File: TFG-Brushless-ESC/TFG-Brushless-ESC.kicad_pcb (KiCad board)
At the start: 4 copper layers, 130 x 50 mm, 113 parts, among them J1 24V IN, J2 MOTOR, J5 USB C Receptacle, J6 HALL SENSORS, J7 SWD, M3 MountingHole_3.2mm_M3_Pad_Via, Q1 TK58E06N1, Q2 TK58E06N1, Q3 TK58E06N1, Q4 TK58E06N1, Q5 TK58E06N1, Q6 TK58E06N1, SW1 BOOT0, SW2 NRST, U1 LM317, U2 LM317, U3 STM32F411CEUx, U4 IR2101, U5 INA180A3, U6 IR2101, U7 INA180A3, U8 IR2101, U9 INA180A3, Y1 25MHz, Y2 32.768kHz

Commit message: temporary unifinished layout
tht components and initia layout
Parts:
- removed C41: 100n, Capacitor_SMD:C_0603_1608Metric
- removed C42: 10p, Capacitor_SMD:C_0603_1608Metric
- removed J7: SWD, Connector_PinHeader_2.54mm:PinHeader_1x04_P2.54mm_Vertical
- removed the M3 at (234.0, 138.0)
- removed the M3 at (234.0, 98.0)
- removed the M3 at (114.0, 98.0)
- removed the M3 at (114.0, 138.0)
- removed R36: 10k, Resistor_SMD:R_0603_1608Metric
- added ?: , , F.Cu at (139.3, 161.1)
- added C11: 100n, Capacitor_SMD:C_0603_1608Metric, F.Cu at (82.1, 175.2)
- added D11: SMAJ16CA-13-F, Diode_SMD:D_SMA, F.Cu at (94.1, 140.9)
- added D12: 1N4148, Diode_SMD:D_SOD-123, F.Cu at (119.1, 132.3)
- added D13: SMAJ16CA-13-F, Diode_SMD:D_SMA, F.Cu at (131.2, 140.8)
- added D5: B240A-13-F, Diode_SMD:D_SMA, F.Cu at (130.0, 149.4)
- added D8: 1N4148, Diode_SMD:D_SOD-123, F.Cu at (54.5, 132.3)
- added F1: 15 A, TFG-Brushless-ESC:Fuseholder_Automotive, F.Cu at (64.9, 153.0)
- added F2: 2A, Fuse:Fuse_1812_4532Metric, F.Cu at (124.5, 153.4)
- added J3: SWD, Connector_PinHeader_2.54mm:PinHeader_1x04_P2.54mm_Vertical, F.Cu at (98.1, 186.9)
- added J4: HALL SENSORS, Connector_JST:JST_PH_B5B-PH-SM4-TB_1x05-1MP_P2.00mm_Vertical, F.Cu at (103.1, 162.2)
- added M3: MountingHole_3.2mm_M3_Pad_Via, MountingHole:MountingHole_3.2mm_M3_Pad_Via, F.Cu at (139.3, 161.1)
- added M3: MountingHole_3.2mm_M3_Pad_Via, MountingHole:MountingHole_3.2mm_M3_Pad_Via, F.Cu at (49.3, 161.1)
- added R13: 10k, Resistor_SMD:R_0603_1608Metric, F.Cu at (100.3, 157.0)
- C13: value 100n -> 20p
- C15: value 20p -> 12p5
- C17: value 12p5 -> 2u2
- C18: value 2u2 -> 10u; footprint Capacitor_SMD:C_0603_1608Metric -> Capacitor_THT:CP_Radial_D5.0mm_P2.00mm
- C19: value 2.2u -> 2u2
- C20: value 100n -> 2.2u; footprint Capacitor_SMD:C_0603_1608Metric -> Capacitor_THT:CP_Radial_D5.0mm_P2.00mm
- C21, C38: value 47u -> 100n; footprint Capacitor_THT:CP_Radial_D5.0mm_P2.00mm -> Capacitor_SMD:C_0603_1608Metric
- C23, C36: value 100n -> 47u; footprint Capacitor_SMD:C_0603_1608Metric -> Capacitor_THT:CP_Radial_D5.0mm_P2.00mm
- C24, C32: value 10u -> 100n; footprint Capacitor_THT:CP_Radial_D5.0mm_P2.00mm -> Capacitor_SMD:C_0603_1608Metric
- C33: value 100n -> 10p
- C34: value 10p -> 2.2u; footprint Capacitor_SMD:C_0603_1608Metric -> Capacitor_THT:CP_Radial_D5.0mm_P2.00mm
- C35: value 2.2u -> 100n; footprint Capacitor_THT:CP_Radial_D5.0mm_P2.00mm -> Capacitor_SMD:C_0603_1608Metric
- C40: value 10u -> 10p; footprint Capacitor_THT:CP_Radial_D5.0mm_P2.00mm -> Capacitor_SMD:C_0603_1608Metric
- D1: value GREEN -> D5V0L2B3T; footprint LED_SMD:LED_0805_2012Metric -> Package_TO_SOT_SMD:SOT-523
- D10: value FERD30H100SB -> 1N4148; footprint Package_TO_SOT_SMD:TO-252-2 -> Diode_SMD:D_SOD-123
- D3: value 1N4148 -> GREEN; footprint Diode_SMD:D_SOD-123 -> LED_SMD:LED_0805_2012Metric
- D6, D9: value 1N4148 -> SMAJ16CA-13-F; footprint Diode_SMD:D_SOD-123 -> Diode_SMD:D_SMA
- D7: value FERD30H100SB -> DESD5V0U1BA; footprint Package_TO_SOT_SMD:TO-252-2 -> Diode_SMD:D_SOD-323_HandSoldering
- J1: value 24V IN -> MOTOR; footprint TerminalBlock_Phoenix:TerminalBlock_Phoenix_MKDS-1,5-2-5.08_1x02_P5.08mm_Horizontal -> TerminalBlock_Phoenix:TerminalBlock_Phoenix_MKDS-1,5-3-5.08_1x03_P5.08mm_Horizontal
- J2: value MOTOR -> USB C Receptacle; footprint TerminalBlock_Phoenix:TerminalBlock_Phoenix_MKDS-1,5-3-5.08_1x03_P5.08mm_Horizontal -> Connector_USB:USB_C_Receptacle_G-Switch_GT-USB-7010ASV
- J5: value USB C Receptacle -> I2C; footprint Connector_USB:USB_C_Receptacle_G-Switch_GT-USB-7010ASV -> Connector_PinHeader_2.54mm:PinHeader_1x04_P2.54mm_Horizontal
- J6: value HALL SENSORS -> 24V IN; footprint Connector_JST:JST_PH_B5B-PH-SM4-TB_1x05-1MP_P2.00mm_Vertical -> TerminalBlock_Phoenix:TerminalBlock_Phoenix_MKDS-1,5-2-5.08_1x02_P5.08mm_Horizontal
- R14, R15, R19, R25, R31: value 1k -> 10k
- R16: value 100R -> 1k; footprint Resistor_SMD:R_0805_2012Metric -> Resistor_SMD:R_0603_1608Metric
- R17, R21, R27, R33: value 10k -> 1k
- R2: value 390R 1% -> 10k
- R20, R26, R32: value 2mR -> 100R; footprint Resistor_SMD:R_2512_6332Metric -> Resistor_SMD:R_0805_2012Metric
- R22, R28: value 100R -> 2mR; footprint Resistor_SMD:R_0805_2012Metric -> Resistor_SMD:R_2512_6332Metric
- R34: value 10k -> 2mR; footprint Resistor_SMD:R_0603_1608Metric -> Resistor_SMD:R_2512_6332Metric
- R5: value 10k -> 390R 1%
- U1: value LM317 -> LM317L_SOT-89; footprint Package_TO_SOT_THT:TO-220-3_Vertical -> Package_TO_SOT_SMD:SOT-89-3
- moved J6 185.1 mm to (56.4, 161.8), turned to 0 degrees
- moved D4 170.4 mm to (49.7, 147.3), turned to 180 degrees
- moved Q1 163.6 mm to (50.4, 123.8), turned to 0 degrees
- moved C21 157.0 mm to (54.2, 135.4)
- moved C20 154.4 mm to (50.4, 136.3)
- moved C22 150.3 mm to (50.4, 130.6)
- moved R18 149.6 mm to (51.3, 126.4), turned to 180 degrees
- moved U4 145.9 mm to (58.5, 132.3), turned to 90 degrees
- moved C24 143.9 mm to (75.8, 126.3), turned to 0 degrees
- moved Q2 139.8 mm to (61.6, 123.8), turned to 0 degrees
- moved R20 135.3 mm to (60.5, 126.4), turned to 0 degrees
- moved C23 133.9 mm to (67.1, 136.1), turned to 0 degrees
- moved U5 127.6 mm to (72.1, 125.3)
- moved R21 126.9 mm to (71.6, 129.6), turned to 0 degrees
- moved C25 121.2 mm to (71.6, 127.9), turned to 180 degrees
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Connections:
- C12 pad 1: /VDDA -> GND
- C12 pad 2: GND -> /BOOT0
- C13 pad 1: GND -> /HSE_1
- C13 pad 2: /NRST -> GND
- C14 pad 1: /HSE_1 -> /HSE_2
- C15 pad 1: /HSE_2 -> /LSE_1
- C16 pad 1: /LSE_1 -> /LSE_2
- C17 pad 1: /LSE_2 -> /VCAP1
- C18 pad 1: /VCAP1 -> +24V
- C19 pad 1: +12V -> +5V
- C21 pad 1: Net-(D3-K) -> +12V
- C21 pad 2: /U -> GND
- C22 pad 1: /U -> Net-(D8-K)
- C22 pad 2: GND -> /U
- C23 pad 1: +3V3 -> /U
- C24 pad 1: +24V -> +3V3
- C25 pad 1: /PA3 -> /PB0
- C26 pad 2: /PA0 -> /PA7
- C29 pad 1: Net-(D6-K) -> Net-(D10-K)
- C32 pad 1: +24V -> /PA4
- C33 pad 1: /PA4 -> GND
- C33 pad 2: GND -> /PA3
- C34 pad 1: GND -> +12V
- C34 pad 2: /PA1 -> GND
- C36 pad 1: +12V -> Net-(D12-K)
- C36 pad 2: GND -> /W
- C37 pad 1: Net-(D9-K) -> /W
- C37 pad 2: /W -> GND
- C38 pad 1: /W -> +3V3
- C39 pad 1: +3V3 -> /PA1
- C40 pad 1: +24V -> GND
- C40 pad 2: GND -> /PA0
- C7 pad 2: /BOOT0 -> /NRST
- D1 pad 1: GND -> /USB_R_N
- D1 pad 2: Net-(D1-A) -> /USB_R_P
- D10 pad 1: /W -> Net-(D10-K)
- D10 pad 2: +24V -> +12V
- D2 pad 1: /PC13 -> GND
- D3 pad 1: Net-(D3-K) -> /PA15
- D3 pad 2: +12V -> Net-(D3-A)
- D4 pad 1: /U -> /24V fused
- D4 pad 3: /U -> /24V fused
- D6 pad 1: Net-(D6-K) -> GND
- D6 pad 2: +12V -> /24V fused
- D7 pad 1: /V -> GND
- D7 pad 2: +24V -> /5V fused
- D9 pad 1: Net-(D9-K) -> GND
- D9 pad 2: +12V -> /U
- J1 pad 1: +24V -> /U
- J1 pad 2: GND -> /V
- J6 pad 1: +3V3 -> GND
- J6 pad 2: /PB1 -> /24V in
- R14 pad 1: +3V3 -> /PA9
- R14 pad 2: Net-(D1-A) -> +3V3
- R15 pad 1: +3V3 -> /PA10
- R15 pad 2: Net-(D2-A) -> +3V3
- R16 pad 1: Net-(U4-HO) -> +3V3
- R16 pad 2: Net-(Q1-G) -> Net-(D2-A)
- R17 pad 1: /PA3 -> +3V3
- R17 pad 2: /U -> Net-(D3-A)
- R18 pad 1: Net-(U4-LO) -> Net-(U4-HO)
- R18 pad 2: Net-(Q2-G) -> Net-(Q1-G)
- R19 pad 1: GND -> /PB0
- R19 pad 2: /PA3 -> /U
- R2 pad 1: Net-(U2-VO) -> GND
- R2 pad 2: Net-(R2-Pad2) -> /NRST
- R20 pad 1: /Half-Bridge-U/Shunt -> Net-(U4-LO)
- R20 pad 2: GND -> Net-(Q2-G)
- R21 pad 1: Net-(R21-Pad1) -> GND
- R21 pad 2: /PA0 -> /PB0
- R22 pad 1: Net-(U6-HO) -> /Half-Bridge-U/Shunt
- R22 pad 2: Net-(Q3-G) -> GND
- R23 pad 1: /PA4 -> Net-(R23-Pad1)
- R23 pad 2: /V -> /PA7
- R24 pad 1: Net-(U6-LO) -> Net-(U6-HO)
- R24 pad 2: Net-(Q4-G) -> Net-(Q3-G)
- R25 pad 1: GND -> /PA4
- R25 pad 2: /PA4 -> /V
- R26 pad 1: /Half-Bridge-V/Shunt -> Net-(U6-LO)
- R26 pad 2: GND -> Net-(Q4-G)
- R27 pad 1: Net-(R27-Pad1) -> GND
- R27 pad 2: /PA1 -> /PA4
- R28 pad 1: Net-(U8-HO) -> /Half-Bridge-V/Shunt
- R28 pad 2: Net-(Q5-G) -> GND
- R29 pad 1: /PA5 -> Net-(R29-Pad1)
- R29 pad 2: /W -> /PA3
- R3 pad 1: Net-(R2-Pad2) -> +12V
- R30 pad 1: Net-(U8-LO) -> Net-(U8-HO)
- R30 pad 2: Net-(Q6-G) -> Net-(Q5-G)
- R31 pad 1: GND -> /PA1
- R31 pad 2: /PA5 -> /W
- R32 pad 1: /Half-Bridge-W/Shunt -> Net-(U8-LO)
- R32 pad 2: GND -> Net-(Q6-G)
- R33 pad 1: Net-(R33-Pad1) -> GND
- R33 pad 2: /PA2 -> /PA1
- R34 pad 1: /PB1 -> /Half-Bridge-W/Shunt
- R34 pad 2: +3V3 -> GND
- R35 pad 1: /PB2 -> Net-(R35-Pad1)
- R35 pad 2: +3V3 -> /PA0
- R4 pad 2: +12V -> Net-(R4-Pad2)
- R5 pad 1: GND -> Net-(R4-Pad2)
- R5 pad 2: /BOOT0 -> /V_DIV_12
- R7 pad 2: +12V -> /V_DIV_12
- R8 pad 2: /NRST -> /BOOT0
- SW1 pad 2: /BOOT0 -> /NRST
- SW2 pad 2: /NRST -> /BOOT0
- U2 pad 1: +12V -> /V_DIV_12
- U2 pad 2: Net-(U2-VO) -> +12V
- U3 pad 44: /NRST -> /BOOT0
- U3 pad 45: /PB8 -> /I2C_SCL
- U3 pad 46: /PB9 -> /I2C_SDA
- U3 pad 7: /BOOT0 -> /NRST
- U4 pad 2: /PA6 -> /PB10
- U4 pad 3: /PA10 -> /PB1
- U4 pad 8: Net-(D3-K) -> Net-(D8-K)
- U5 pad 1: Net-(R21-Pad1) -> Net-(R23-Pad1)
- U6 pad 2: /PA7 -> /PA6
- U6 pad 3: /PA9 -> /PA5
- U6 pad 8: Net-(D6-K) -> Net-(D10-K)
- U7 pad 1: Net-(R27-Pad1) -> Net-(R29-Pad1)
- U8 pad 2: /PB0 -> /PB7
- U8 pad 3: /PA8 -> /PB6
- U8 pad 8: Net-(D9-K) -> Net-(D12-K)
- U9 pad 1: Net-(R33-Pad1) -> Net-(R35-Pad1)
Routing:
- net /PB10: track 134.1 -> 0.00 mm
- net /PB2: track 127.2 -> 0.00 mm
- net GND: track 222.5 -> 99.8 mm, vias 39 -> 35
- net /PB1: track 117.5 -> 0.00 mm
- net +12V: track 67.8 -> 25.1 mm
- net +24V: track 9.15 -> 36.4 mm, vias 15 -> 12
- net +5V: track 25.3 -> 42.0 mm, vias 2 -> 0
- net /PC13: track 13.8 -> 0.00 mm, vias 2 -> 0
- net /V: track 44.5 -> 31.1 mm, vias 4 -> 14
- net /W: track 44.5 -> 31.2 mm, vias 4 -> 14
- net +3V3: track 116.4 -> 103.3 mm, vias 12 -> 0
- net /PA5: track 12.9 -> 0.00 mm, vias 1 -> 0
- net Net-(D3-K): track 12.7 -> 0.00 mm
- net Net-(D9-K): track 12.7 -> 0.00 mm
- net Net-(D6-K): track 12.7 -> 0.00 mm
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- added copper zone on F.Cu, net +12V
- added copper zone on F.Cu, net /24V fused
- added copper zone on F.Cu, net /24V in
- added copper zone on F.Cu, net /5V fused
- added copper zone on F.Cu, net VDC
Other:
- board size 130 x 50 mm -> 100 x 46 mm
- board text added: "24V In"
- board text added: "OUT"
- board text added: "Reg 12V"
- board text added: "Reg 5V"
- board text added: "U"
- board text added: "USB C"
- board text added: "V"
- board text added: "W"
- board text added: "uC"

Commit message: cleaned layout
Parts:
- removed ?: , 
- removed C1, C10, C11, C12, C21, C24, C25, C28, C31, C32, C35, C38, C39, C4, C7, C8, C9: 100n, Capacitor_SMD:C_0603_1608Metric
- removed C13, C14: 20p, Capacitor_SMD:C_0603_1608Metric
- removed C15, C16: 12p5, Capacitor_SMD:C_0603_1608Metric
- removed C17: 2u2, Capacitor_SMD:C_0603_1608Metric
- removed C18, C3, C6: 10u, Capacitor_THT:CP_Radial_D5.0mm_P2.00mm
- removed C19: 2u2, Capacitor_THT:CP_Radial_D5.0mm_P2.00mm
- removed C2, C5: 220u, Capacitor_THT:CP_Radial_D5.0mm_P2.00mm
- removed C20, C27, C34: 2.2u, Capacitor_THT:CP_Radial_D5.0mm_P2.00mm
- removed C22, C23, C29, C30, C36, C37: 47u, Capacitor_THT:CP_Radial_D5.0mm_P2.00mm
- removed C26, C33, C40: 10p, Capacitor_SMD:C_0603_1608Metric
- removed D1: D5V0L2B3T, Package_TO_SOT_SMD:SOT-523
- removed D10, D12, D8: 1N4148, Diode_SMD:D_SOD-123
- removed D11, D13, D6, D9: SMAJ16CA-13-F, Diode_SMD:D_SMA
- removed D2, D3: GREEN, LED_SMD:LED_0805_2012Metric
- removed D4: FERD30H100SB, Package_TO_SOT_SMD:TO-252-2
- removed D5: B240A-13-F, Diode_SMD:D_SMA
- removed D7: DESD5V0U1BA, Diode_SMD:D_SOD-323_HandSoldering
- removed F1: 15 A, TFG-Brushless-ESC:Fuseholder_Automotive
- removed F2: 2A, Fuse:Fuse_1812_4532Metric
- removed J1: MOTOR, TerminalBlock_Phoenix:TerminalBlock_Phoenix_MKDS-1,5-3-5.08_1x03_P5.08mm_Horizontal
- removed J2: USB C Receptacle, Connector_USB:USB_C_Receptacle_G-Switch_GT-USB-7010ASV
- removed J3: SWD, Connector_PinHeader_2.54mm:PinHeader_1x04_P2.54mm_Vertical
- removed J4: HALL SENSORS, Connector_JST:JST_PH_B5B-PH-SM4-TB_1x05-1MP_P2.00mm_Vertical
- removed J5: I2C, Connector_PinHeader_2.54mm:PinHeader_1x04_P2.54mm_Horizontal
- removed J6: 24V IN, TerminalBlock_Phoenix:TerminalBlock_Phoenix_MKDS-1,5-2-5.08_1x02_P5.08mm_Horizontal
- removed L1: 10u, Inductor_SMD:L_0805_2012Metric
- removed M3 (x2): MountingHole_3.2mm_M3_Pad_Via, MountingHole:MountingHole_3.2mm_M3_Pad_Via
- removed Q1, Q2, Q3, Q4, Q5, Q6: TK58E06N1, Package_TO_SOT_THT:TO-220-3_Vertical
- removed R1: 240R 1%, Resistor_SMD:R_0603_1608Metric
- removed R10, R9: 5k1, Resistor_SMD:R_0603_1608Metric
- removed R11, R12: 22R, Resistor_SMD:R_0603_1608Metric
- removed R13, R14, R15, R19, R2, R23, R25, R29, R31, R35, R8: 10k, Resistor_SMD:R_0603_1608Metric
- removed R16, R17, R21, R27, R33: 1k, Resistor_SMD:R_0603_1608Metric
- removed R18, R20, R24, R26, R30, R32: 100R, Resistor_SMD:R_0805_2012Metric
- removed R22, R28, R34: 2mR, Resistor_SMD:R_2512_6332Metric
- removed R3, R4, R5, R6: 390R 1%, Resistor_SMD:R_0603_1608Metric
- removed R7: 10k 1%, Resistor_SMD:R_0603_1608Metric
- removed SW1: BOOT0, Button_Switch_SMD:SW_Push_1P1T_NO_6x6mm_H9.5mm
- removed SW2: NRST, Button_Switch_SMD:SW_Push_1P1T_NO_6x6mm_H9.5mm
- removed U1: LM317L_SOT-89, Package_TO_SOT_SMD:SOT-89-3
- removed U2: LM317, Package_TO_SOT_THT:TO-220-3_Vertical
- removed U3: STM32F411CEUx, Package_DFN_QFN:QFN-48-1EP_7x7mm_P0.5mm_EP5.6x5.6mm
- removed U4, U6, U8: IR2101, Package_SO:SOIC-8-1EP_3.9x4.9mm_P1.27mm_EP2.29x3mm
- removed U5, U7, U9: INA180A3, Package_TO_SOT_SMD:SOT-23-5
- removed Y1: 25MHz, Oscillator:Oscillator_SMD_Abracon_ASE-4Pin_3.2x2.5mm
- removed Y2: 32.768kHz, Oscillator:Oscillator_SMD_Abracon_ASE-4Pin_3.2x2.5mm
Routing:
- net +3V3: track 103.3 -> 0.00 mm
- net GND: track 99.8 -> 0.00 mm, vias 35 -> 0
- net +5V: track 42.0 -> 0.00 mm
- net +24V: track 36.4 -> 0.00 mm, vias 12 -> 0
- net /W: track 31.2 -> 0.00 mm, vias 14 -> 0
- net /U: track 31.1 -> 0.00 mm, vias 14 -> 0
- net /V: track 31.1 -> 0.00 mm, vias 14 -> 0
- net +12V: track 25.1 -> 0.00 mm
- net /BOOT0: track 19.5 -> 0.00 mm
- net /HSE_2: track 17.1 -> 0.00 mm
- net /LSE_2: track 16.2 -> 0.00 mm
- net /HSE_1: track 14.2 -> 0.00 mm
- net /LSE_1: track 14.1 -> 0.00 mm
- net /NRST: track 13.5 -> 0.00 mm, vias 1 -> 0
- net VDC: track 10.5 -> 0.00 mm, vias 2 -> 0
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- removed copper zone on F.Cu, net +12V
- removed copper zone on B.Cu, net +24V
- removed copper zone on F.Cu, net +24V
- removed copper zone on F.Cu, net /24V fused
- removed copper zone on F.Cu, net /24V in
- removed copper zone on F.Cu, net /5V fused
- removed copper zone on F.Cu, net /Half-Bridge-U/Shunt
- removed copper zone on F.Cu, net /Half-Bridge-V/Shunt
- removed copper zone on F.Cu, net /Half-Bridge-W/Shunt
- removed copper zone on B.Cu, net /U
- removed copper zone on F.Cu, net /U
- removed copper zone on B.Cu, net /V
- removed copper zone on F.Cu, net /V
- removed copper zone on B.Cu, net /W
- removed copper zone on F.Cu, net /W
- removed copper zone on F.Cu, net GND
- removed copper zone on F.Cu, net VDC

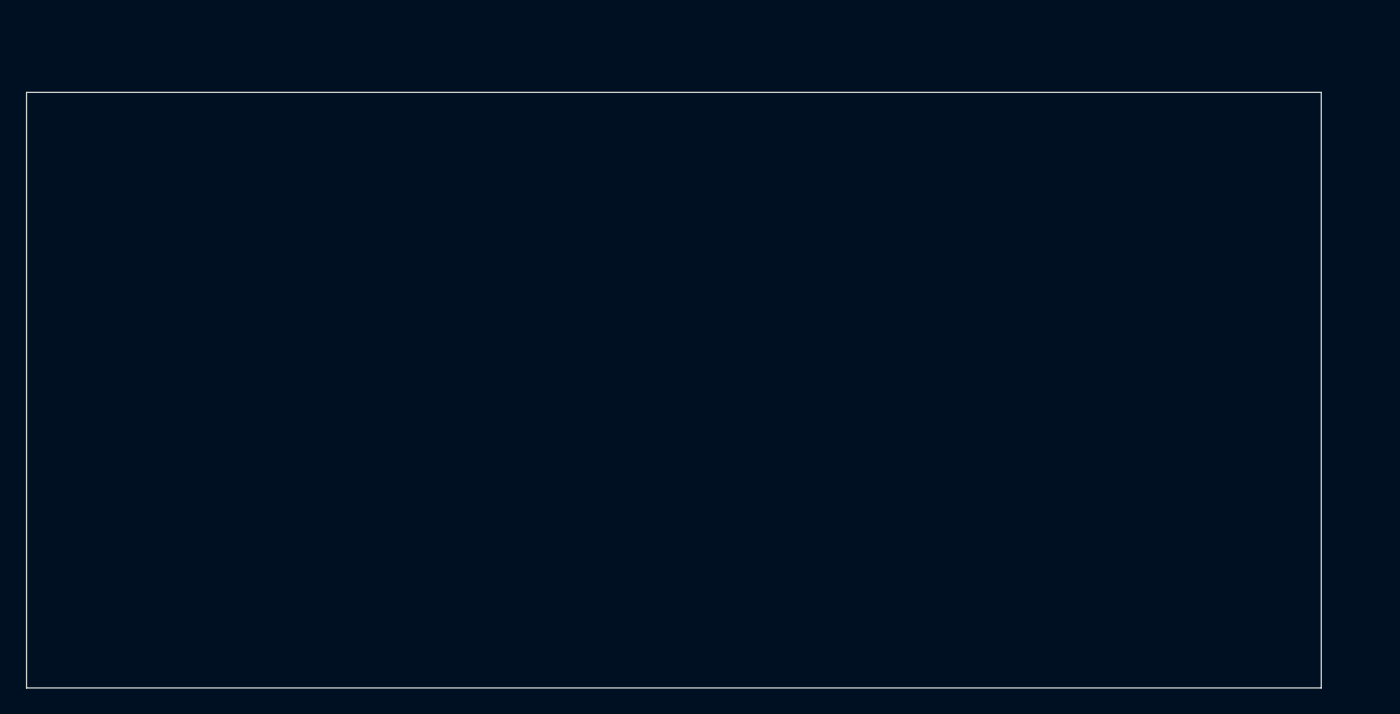
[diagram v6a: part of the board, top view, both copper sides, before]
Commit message: updated code to match pinout
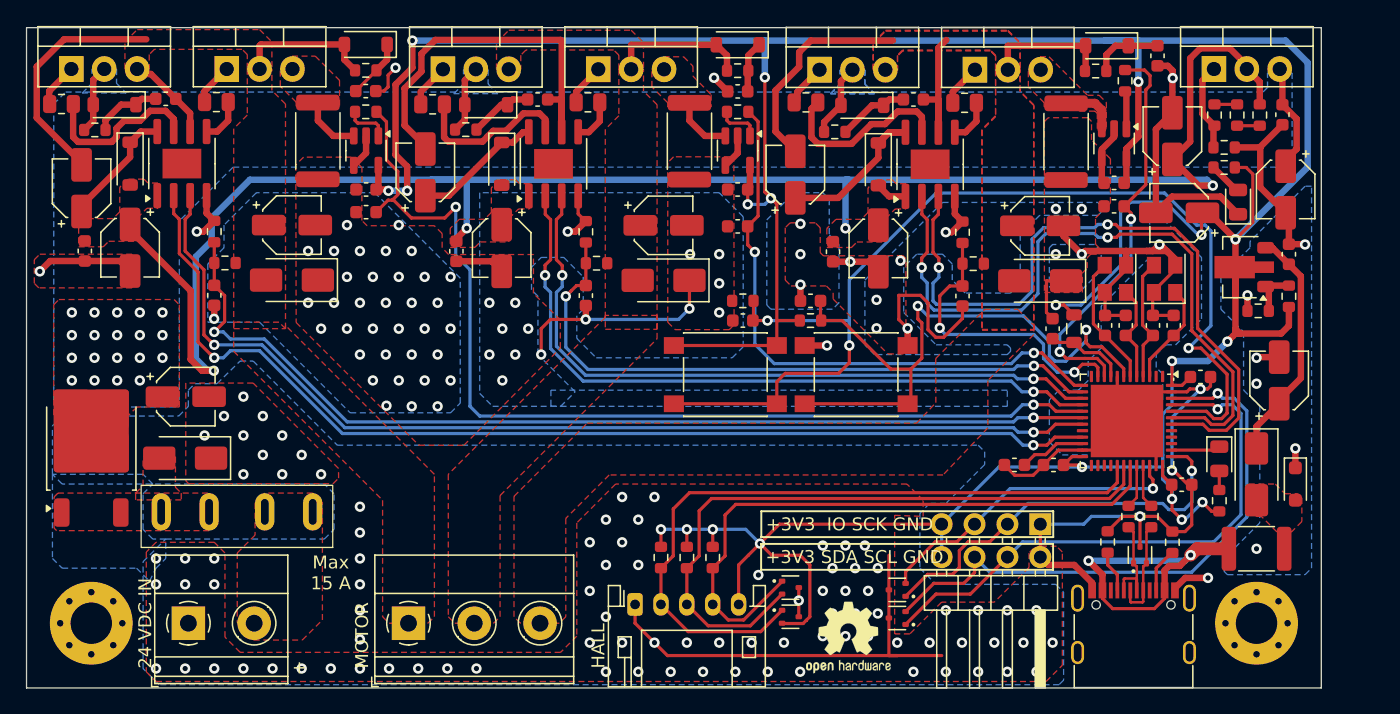
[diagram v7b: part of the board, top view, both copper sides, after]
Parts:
- added C1: 100n, Capacitor_SMD:C_0603_1608Metric, F.Cu at (141.8, 133.0)
- added C10: 100n, Capacitor_SMD:C_0603_1608Metric, F.Cu at (123.5, 138.8)
- added C11: 100n, Capacitor_SMD:C_0603_1608Metric, F.Cu at (104.8, 136.6)
- added C12: 20p, Capacitor_SMD:C_0603_1608Metric, F.Cu at (129.2, 138.5)
- added C13: 20p, Capacitor_SMD:C_0603_1608Metric, F.Cu at (127.6, 138.5)
- added C14: 12p5, Capacitor_SMD:C_0603_1608Metric, F.Cu at (132.9, 138.5)
- added C15: 12p5, Capacitor_SMD:C_0603_1608Metric, F.Cu at (131.3, 138.5)
- added C16: 2u2, Capacitor_SMD:C_0603_1608Metric, F.Cu at (120.6, 149.3)
- added C17: 10u, Capacitor_SMD:CP_Elec_4x5.4, F.Cu at (56.6, 144.0)
- added C18: 2u2, Capacitor_SMD:CP_Elec_4x5.4, F.Cu at (141.0, 142.8)
- added C19: 2.2u, Capacitor_SMD:CP_Elec_4x5.4, F.Cu at (52.3, 132.5)
- added C2: 10u, Capacitor_SMD:CP_Elec_4x5.4, F.Cu at (133.3, 129.8)
- added C20: 100n, Capacitor_SMD:C_0603_1608Metric, F.Cu at (48.8, 132.8)
- added C21: 3n3, Capacitor_SMD:C_0603_1608Metric, F.Cu at (55.0, 121.0)
- added C22: 47u, Capacitor_SMD:CP_Elec_4x5.4, F.Cu at (48.5, 127.9)
- added C23: 47u, Capacitor_SMD:CP_Elec_4x5.4, F.Cu at (64.8, 130.8)
- added C24: 100n, Capacitor_SMD:C_0603_1608Metric, F.Cu at (70.5, 128.0)
- added C25: 3n3, Capacitor_SMD:C_0603_1608Metric, F.Cu at (70.5, 120.4)
- added C26: 100n, Capacitor_SMD:C_0603_1608Metric, F.Cu at (58.8, 136.2)
- added C27: 10p, Capacitor_SMD:C_0603_1608Metric, F.Cu at (70.5, 129.8)
- added C28: 2.2u, Capacitor_SMD:CP_Elec_4x5.4, F.Cu at (81.0, 132.5)
- added C29: 100n, Capacitor_SMD:C_0603_1608Metric, F.Cu at (77.5, 132.8)
- added C3: 100n, Capacitor_SMD:C_0603_1608Metric, F.Cu at (141.3, 122.3)
- added C30: 3n3, Capacitor_SMD:C_0603_1608Metric, F.Cu at (83.8, 121.1)
- added C31: 47u, Capacitor_SMD:CP_Elec_4x5.4, F.Cu at (75.1, 126.7)
- added C32: 47u, Capacitor_SMD:CP_Elec_4x5.4, F.Cu at (93.5, 130.8)
- added C33: 100n, Capacitor_SMD:C_0603_1608Metric, F.Cu at (99.2, 128.0)
- added C34: 3n3, Capacitor_SMD:C_0603_1608Metric, F.Cu at (99.2, 120.5)
- added C35: 100n, Capacitor_SMD:C_0603_1608Metric, F.Cu at (87.5, 136.2)
- added C36: 10p, Capacitor_SMD:C_0603_1608Metric, F.Cu at (99.2, 130.9)
- added C37: 2.2u, Capacitor_SMD:CP_Elec_4x5.4, F.Cu at (110.1, 132.6)
- added C38: 100n, Capacitor_SMD:C_0603_1608Metric, F.Cu at (106.6, 132.8)
- added C39: 3n3, Capacitor_SMD:C_0603_1608Metric, F.Cu at (112.8, 121.1)
- added C4: 220u, Capacitor_SMD:CP_Elec_4x5.4, F.Cu at (141.5, 128.0)
- added C40: 47u, Capacitor_SMD:CP_Elec_4x5.4, F.Cu at (103.7, 126.9)
- added C41: 47u, Capacitor_SMD:CP_Elec_4x5.4, F.Cu at (122.6, 130.8)
- added C42: 100n, Capacitor_SMD:C_0603_1608Metric, F.Cu at (128.3, 127.5)
- added C43: 3n3, Capacitor_SMD:C_0603_1608Metric, F.Cu at (131.6, 117.7)
- added C44: 100n, Capacitor_SMD:C_0603_1608Metric, F.Cu at (116.6, 136.3)
- added C45: 10p, Capacitor_SMD:C_0603_1608Metric, F.Cu at (128.3, 129.3)
- added C5: 10u, Capacitor_SMD:CP_Elec_4x5.4, F.Cu at (132.8, 123.9)
- added C6: 100n, Capacitor_SMD:C_0603_1608Metric, F.Cu at (99.6, 138.2)
- added C7: 100n, Capacitor_SMD:C_0603_1608Metric, F.Cu at (133.5, 150.8)
- added C8: 100n, Capacitor_SMD:C_0603_1608Metric, F.Cu at (123.6, 149.3)
- added C9: 100n, Capacitor_SMD:C_0603_1608Metric, F.Cu at (134.9, 142.5)
- added D1: D5V0L2B3T, Package_TO_SOT_SMD:SOT-523, F.Cu at (111.5, 159.0)
- added D10: SMAJ16CA-13-F, Diode_SMD:D_SMA, F.Cu at (56.5, 148.8)
- added D11: DESD5V0U1BA, Diode_SMD:D_SOD-323_HandSoldering, F.Cu at (142.3, 150.8)
- added D12: 1N4148, Diode_SMD:D_SOD-123, F.Cu at (51.1, 121.5)
- added D13: 1N4148, Diode_SMD:D_SOD-123, F.Cu at (52.3, 126.0)
- added D14: 1N4148, Diode_SMD:D_SOD-123, F.Cu at (70.5, 116.8)
- added D15: SMAJ16CA-13-F, Diode_SMD:D_SMA, F.Cu at (64.8, 135.0)
- added D16: 1N4148, Diode_SMD:D_SOD-123, F.Cu at (79.8, 121.5)
- added D17: 1N4148, Diode_SMD:D_SOD-123, F.Cu at (81.0, 126.0)
- added D18: 1N4148, Diode_SMD:D_SOD-123, F.Cu at (99.2, 116.9)
- added D19: SMAJ16CA-13-F, Diode_SMD:D_SMA, F.Cu at (93.5, 135.0)
- added D2: D5V0L2B3T, Package_TO_SOT_SMD:SOT-523, F.Cu at (130.3, 156.3)
- added D20: 1N4148, Diode_SMD:D_SOD-123, F.Cu at (108.8, 121.5)
- added D21: 1N4148, Diode_SMD:D_SOD-123, F.Cu at (110.1, 126.1)
- added D22: 1N4148, Diode_SMD:D_SOD-123, F.Cu at (127.7, 116.9)
- added D23: SMAJ16CA-13-F, Diode_SMD:D_SMA, F.Cu at (122.6, 135.1)
- added D3: D5V0L2B3T, Package_TO_SOT_SMD:SOT-523, F.Cu at (103.3, 158.8)
- added D4: D5V0L2B3T, Package_TO_SOT_SMD:SOT-523, F.Cu at (103.3, 161.0)
- added D5: D5V0L2B3T, Package_TO_SOT_SMD:SOT-523, F.Cu at (111.5, 161.1)
- added D6: GREEN, LED_SMD:LED_0805_2012Metric, F.Cu at (137.9, 129.0)
- added D7: GREEN, LED_SMD:LED_0805_2012Metric, F.Cu at (136.4, 148.8)
- added D8: FERD30H100SB, Package_TO_SOT_SMD:TO-252-2, F.Cu at (49.3, 147.9)
- added D9: B240A-13-F, Diode_SMD:D_SMA, F.Cu at (139.3, 150.0)
- added F1: 15 A, TFG-Brushless-ESC:Fuseholder_Automotive, F.Cu at (66.4, 152.9)
- added F2: 2A, Fuse:Fuse_1812_4532Metric, F.Cu at (139.3, 155.8)
- added J1: MOTOR, TerminalBlock_Phoenix:TerminalBlock_Phoenix_MKDS-1,5-3-5.08_1x03_P5.08mm_Horizontal, F.Cu at (73.8, 161.5)
- added J2: USB C Receptacle, Connector_USB:USB_C_Receptacle_G-Switch_GT-USB-7010ASV, F.Cu at (129.8, 162.7)
- added J3: HALL SENSORS, Connector_JST:JST_PH_S5B-PH-K_1x05_P2.00mm_Horizontal, F.Cu at (91.3, 160.1)
- added J4: SWD-I2C, Connector_PinHeader_2.54mm:PinHeader_2x04_P2.54mm_Horizontal, F.Cu at (122.6, 153.9)
- added J5: 24V IN, TerminalBlock_Phoenix:TerminalBlock_Phoenix_MKDS-1,5-2-5.08_1x02_P5.08mm_Horizontal, F.Cu at (56.8, 161.5)
- added L1: 10u, Inductor_SMD:L_0805_2012Metric, F.Cu at (125.2, 138.8)
- added Q1: TK58E06N1, Package_TO_SOT_THT:TO-220-3_Vertical, F.Cu at (47.7, 118.7)
- added Q2: TK58E06N1, Package_TO_SOT_THT:TO-220-3_Vertical, F.Cu at (59.7, 118.7)
- added Q3: TK58E06N1, Package_TO_SOT_THT:TO-220-3_Vertical, F.Cu at (76.4, 118.7)
- added Q4: TK58E06N1, Package_TO_SOT_THT:TO-220-3_Vertical, F.Cu at (88.4, 118.7)
- added Q5: TK58E06N1, Package_TO_SOT_THT:TO-220-3_Vertical, F.Cu at (105.5, 118.8)
- added Q6: TK58E06N1, Package_TO_SOT_THT:TO-220-3_Vertical, F.Cu at (117.5, 118.8)
- added R1: 240R 1%, Resistor_SMD:R_0603_1608Metric, F.Cu at (141.8, 136.3)
- added R10: 5k1, Resistor_SMD:R_0603_1608Metric, F.Cu at (132.8, 155.3)
- added R11: 22R, Resistor_SMD:R_0603_1608Metric, F.Cu at (129.4, 153.3)
- added R12: 22R, Resistor_SMD:R_0603_1608Metric, F.Cu at (131.1, 153.3)
- added R13: 10k, Resistor_SMD:R_0603_1608Metric, F.Cu at (97.3, 156.5)
- added R14: 10k, Resistor_SMD:R_0603_1608Metric, F.Cu at (95.3, 156.5)
- added R15: 10k, Resistor_SMD:R_0603_1608Metric, F.Cu at (93.3, 156.5)
- added R16: 1k, Resistor_SMD:R_0603_1608Metric, F.Cu at (136.8, 126.3)
- added R17: 1k, Resistor_SMD:R_0603_1608Metric, F.Cu at (136.4, 152.1)
- added R18: 220R, Resistor_SMD:R_0603_1608Metric, F.Cu at (49.6, 123.4)
- added R19: 100R, Resistor_SMD:R_0805_2012Metric, F.Cu at (47.0, 121.4)
- added R2: 10k, Resistor_SMD:R_0603_1608Metric, F.Cu at (99.6, 136.6)
- added R20: 220R, Resistor_SMD:R_0603_1608Metric, F.Cu at (70.5, 118.8)
- added R21: 10k, Resistor_SMD:R_0603_1608Metric, F.Cu at (59.6, 133.7)
- added R22: 100R, Resistor_SMD:R_0805_2012Metric, F.Cu at (58.9, 121.3)
- added R23: 1k, Resistor_SMD:R_0603_1608Metric, F.Cu at (58.8, 131.3)
- added R24: 2mR, Resistor_SMD:R_2512_6332Metric, F.Cu at (66.8, 124.3)
- added R25: 10k, Resistor_SMD:R_0603_1608Metric, F.Cu at (70.5, 122.0)
- added R26: 220R, Resistor_SMD:R_0603_1608Metric, F.Cu at (78.2, 123.4)
- added R27: 100R, Resistor_SMD:R_0805_2012Metric, F.Cu at (75.6, 121.5)
- added R28: 220R, Resistor_SMD:R_0603_1608Metric, F.Cu at (99.2, 118.9)
- added R29: 10k, Resistor_SMD:R_0603_1608Metric, F.Cu at (88.3, 133.7)
- added R3: 390R 1%, Resistor_SMD:R_0603_1608Metric, F.Cu at (139.5, 122.3)
- added R30: 100R, Resistor_SMD:R_0805_2012Metric, F.Cu at (87.6, 121.3)
- added R31: 1k, Resistor_SMD:R_0603_1608Metric, F.Cu at (87.5, 131.3)
- added R32: 2mR, Resistor_SMD:R_2512_6332Metric, F.Cu at (95.5, 124.3)
- added R33: 10k, Resistor_SMD:R_0603_1608Metric, F.Cu at (99.2, 122.0)
- added R34: 220R, Resistor_SMD:R_0603_1608Metric, F.Cu at (106.7, 123.6)
- added R35: 100R, Resistor_SMD:R_0805_2012Metric, F.Cu at (104.5, 121.3)
- added R36: 220R, Resistor_SMD:R_0603_1608Metric, F.Cu at (126.9, 118.9)
- added R37: 10k, Resistor_SMD:R_0603_1608Metric, F.Cu at (117.4, 133.8)
- added R38: 100R, Resistor_SMD:R_0805_2012Metric, F.Cu at (116.7, 121.3)
- added R39: 1k, Resistor_SMD:R_0603_1608Metric, F.Cu at (116.6, 131.3)
- added R4: 390R 1%, Resistor_SMD:R_0603_1608Metric, F.Cu at (137.8, 122.3)
- added R40: 2mR, Resistor_SMD:R_2512_6332Metric, F.Cu at (124.6, 124.3)
- added R41: 10k, Resistor_SMD:R_0603_1608Metric, F.Cu at (129.1, 119.6)
- added R5: 390R 1%, Resistor_SMD:R_0603_1608Metric, F.Cu at (136.0, 122.3)
- added R6: 390R 1%, Resistor_SMD:R_0603_1608Metric, F.Cu at (139.4, 137.4)
- added R7: 10k 1%, Resistor_SMD:R_0603_1608Metric, F.Cu at (136.8, 124.8)
- added R8: 10k, Resistor_SMD:R_0603_1608Metric, F.Cu at (104.8, 138.2)
- added R9: 5k1, Resistor_SMD:R_0603_1608Metric, F.Cu at (127.8, 155.3)
- added REF**: MountingHole_3.2mm_M3_Pad_Via, MountingHole:MountingHole_3.2mm_M3_Pad_Via, F.Cu at (139.3, 161.5)
- added REF**: MountingHole_3.2mm_M3_Pad_Via, MountingHole:MountingHole_3.2mm_M3_Pad_Via, F.Cu at (49.3, 161.5)
- added REF**: OSHW-Logo2_7.3x6mm_SilkScreen, Symbol:OSHW-Logo2_7.3x6mm_SilkScreen, F.Cu at (107.8, 162.6)
- added REF**: KiCad-Logo2_5mm_SilkScreen, Symbol:KiCad-Logo2_5mm_SilkScreen, B.Cu at (116.8, 162.5)
- added SW1: BOOT0, Button_Switch_SMD:SW_Push_1P1T_NO_6x6mm_H9.5mm, F.Cu at (98.3, 142.3)
- added SW2: NRST, Button_Switch_SMD:SW_Push_1P1T_NO_6x6mm_H9.5mm, F.Cu at (108.4, 142.3)
- added U1: LM317L_SOT-89, Package_TO_SOT_SMD:SOT-89-3, F.Cu at (138.0, 134.0)
- added U2: LM317, Package_TO_SOT_THT:TO-220-3_Vertical, F.Cu at (136.0, 118.7)
- added U3: STM32F411CEUx, Package_DFN_QFN:QFN-48-1EP_7x7mm_P0.5mm_EP5.6x5.6mm, F.Cu at (129.3, 145.9)
- added U4: IR2101, Package_SO:SOIC-8-1EP_3.9x4.9mm_P1.27mm_EP2.29x3mm, F.Cu at (56.3, 126.0)
- added U5: INA180A3, Package_TO_SOT_SMD:SOT-23-5, F.Cu at (70.5, 125.0)
- added U6: IR2101, Package_SO:SOIC-8-1EP_3.9x4.9mm_P1.27mm_EP2.29x3mm, F.Cu at (85.0, 126.0)
- added U7: INA180A3, Package_TO_SOT_SMD:SOT-23-5, F.Cu at (99.2, 125.0)
- added U8: IR2101, Package_SO:SOIC-8-1EP_3.9x4.9mm_P1.27mm_EP2.29x3mm, F.Cu at (114.1, 126.1)
- added U9: INA180A3, Package_TO_SOT_SMD:SOT-23-5, F.Cu at (128.3, 124.5)
- added Y1: 25MHz, Oscillator:Oscillator_SMD_Abracon_ASE-4Pin_3.2x2.5mm, F.Cu at (128.4, 134.9)
- added Y2: 32.768kHz, Oscillator:Oscillator_SMD_Abracon_ASE-4Pin_3.2x2.5mm, F.Cu at (132.2, 134.9)
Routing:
- net +3V3: track 0.00 -> 303.3 mm, vias 0 -> 20
- net GND: track 0.00 -> 252.7 mm, vias 0 -> 172
- net +12V: track 0.00 -> 142.0 mm, vias 0 -> 4
- net /BOOT0: track 0.00 -> 86.4 mm, vias 0 -> 3
- net /PB10: track 0.00 -> 84.4 mm, vias 0 -> 2
- net /PB1: track 0.00 -> 82.7 mm, vias 0 -> 2
- net /PA7: track 0.00 -> 79.2 mm, vias 0 -> 2
- net /PB0: track 0.00 -> 77.7 mm, vias 0 -> 2
- net /PA6: track 0.00 -> 55.2 mm, vias 0 -> 2
- net /PA8: track 0.00 -> 55.1 mm
- net /PB6: track 0.00 -> 54.9 mm, vias 0 -> 2
- net /PA5: track 0.00 -> 54.4 mm, vias 0 -> 2
- net /PB7: track 0.00 -> 54.1 mm, vias 0 -> 2
- net /PA9: track 0.00 -> 51.8 mm
- net /PA4: track 0.00 -> 50.7 mm, vias 0 -> 2
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- added copper zone on F.Cu, net +12V
- added copper zone on B.Cu, net +24V
- added copper zone on F.Cu, net +24V
- added copper zone on F.Cu, net /24V fused
- added copper zone on F.Cu, net /24V in
- added copper zone on F.Cu, net /5V fused
- added copper zone on F.Cu, net /Half-Bridge-U/Shunt
- added copper zone on F.Cu, net /Half-Bridge-V/Shunt
- added copper zone on F.Cu, net /Half-Bridge-W/Shunt
- added copper zone on F.Cu, net /U
- added copper zone on F.Cu, net /V
- added copper zone on F.Cu, net /W
- added copper zone on B.Cu, net GND
- added copper zone on F.Cu, net GND
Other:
- board size 100 x 46 mm -> 100 x 51 mm
- board text added: "+"
- board text added: "+3V3 IO SCK GND"
- board text added: "+3V3 SDA SCL GND"
- board text added: "24 VDC IN"
- board text added: "Designed by humans on Earth"
- board text added: "Dimensions: 100 x 51 mm Distance between screw holes: 90 mm"
- board text added: "HALL"
- board text added: "MOTOR"
- board text added: "Max 15 A"
- board text added: "Mira a la pizarra"
- board text added: "github.com/AdriTeixeHax"

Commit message: Added pulldown resistors at motor output
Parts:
- removed C23, C32, C41: 47u, Capacitor_SMD:CP_Elec_4x5.4
- added R42: 10k, Resistor_SMD:R_0603_1608Metric, F.Cu at (64.7, 129.3)
- added R43: 10k, Resistor_SMD:R_0603_1608Metric, F.Cu at (93.3, 129.3)
- added R44: 10k, Resistor_SMD:R_0603_1608Metric, F.Cu at (122.5, 129.3)
- F1: value 15 A -> 15A
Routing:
- net GND: track 252.7 -> 242.3 mm, vias 172 -> 171
